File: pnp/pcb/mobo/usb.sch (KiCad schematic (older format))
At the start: 15 parts, among them J41 USB_B, J42 USB_A, J43 USB_A, J44 USB_A, U6 CH340G, U8 FE1.1S, Y2 12MHz, Y3 12MHz

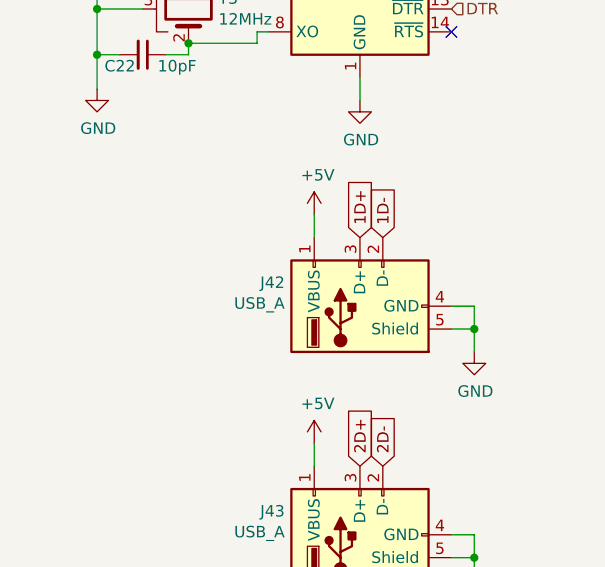
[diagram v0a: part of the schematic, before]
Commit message: Removing KiCad cache and bak files. Removing fabrication outputs. Updated Marlin to use the correct stepper driver for the Z and Y axis.
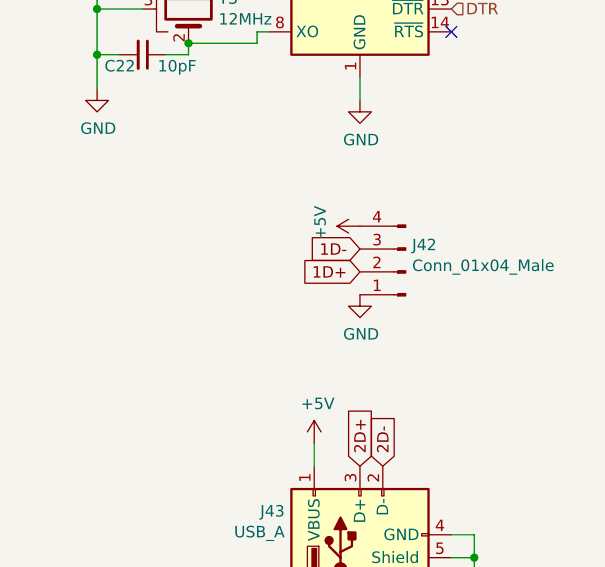
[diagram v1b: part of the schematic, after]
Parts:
- removed J42: USB_A, Connector_USB:USB_A_CNCTech_1001-011-01101_Horizontal, symbol Connector:USB_A
- added J42: Conn_01x04_Male, Connector_PinHeader_2.54mm:PinHeader_1x04_P2.54mm_Vertical, symbol Connector:Conn_01x04_Male
- J43, J44: footprint Connector_USB:USB_A_CNCTech_1001-011-01101_Horizontal -> Connector_USB:USB_A_Wuerth_61400826021_Horizontal_Stacked
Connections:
- net +5V: now also J42.4 (Pin_4)
- net 1D+: now also J42.2 (Pin_2)
- net 1D-: now also J42.3 (Pin_3)
- net GND: now also J42.1 (Pin_1)
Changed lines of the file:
@@
-$EndComp
-$Comp
-L Connector:USB_A J42
-U 1 1 5EB35624
-P 8650 3400
-F 0 "J42" V 8753 3729 50  0000 L CNN
-F 1 "USB_A" V 8662 3729 50  0000 L CNN
-F 2 "Connector_USB:USB_A_CNCTech_1001-011-01101_Horizontal" H 8800 3350 50  0001 C CNN
-F 3 " ~" H 8800 3350 50  0001 C CNN
-	1    8650 3400
-	0    -1   -1   0
 $EndComp
 $Comp
@@
 L power:GND #PWR0235
 U 1 1 5EB47F0D
-P 9150 3600
-F 0 "#PWR0235" H 9150 3350 50  0001 C CNN
-F 1 "GND" H 9155 3427 50  0000 C CNN
-F 2 "" H 9150 3600 50  0001 C CNN
-F 3 "" H 9150 3600 50  0001 C CNN
-	1    9150 3600
+P 8650 3350
+F 0 "#PWR0235" H 8650 3100 50  0001 C CNN
+F 1 "GND" H 8655 3177 50  0000 C CNN
+F 2 "" H 8650 3350 50  0001 C CNN
+F 3 "" H 8650 3350 50  0001 C CNN
+	1    8650 3350
 	1    0    0    -1
 $EndComp
@@
 	1    0    0    -1
 $EndComp
-Wire Wire Line
-	9150 3600 9150 3500
-Wire Wire Line
-	9150 3500 9050 3500
-Wire Wire Line
-	9150 3500 9150 3400
-Wire Wire Line
-	9150 3400 9050 3400
-Connection ~ 9150 3500
 $Comp
 L Connector:USB_A J43
@@
 F 0 "J43" V 8753 4729 50  0000 L CNN
 F 1 "USB_A" V 8662 4729 50  0000 L CNN
-F 2 "Connector_USB:USB_A_CNCTech_1001-011-01101_Horizontal" H 8800 4350 50  0001 C CNN
+F 2 "Connector_USB:USB_A_Wuerth_61400826021_Horizontal_Stacked" H 8800 4350 50  0001 C CNN
 F 3 " ~" H 8800 4350 50  0001 C CNN
 	1    8650 4400
@@
 F 0 "J44" V 8753 5879 50  0000 L CNN
 F 1 "USB_A" V 8662 5879 50  0000 L CNN
-F 2 "Connector_USB:USB_A_CNCTech_1001-011-01101_Horizontal" H 8800 5500 50  0001 C CNN
+F 2 "Connector_USB:USB_A_Wuerth_61400826021_Horizontal_Stacked" H 8800 5500 50  0001 C CNN
 F 3 " ~" H 8800 5500 50  0001 C CNN
 	1    8650 5550
@@
 L power:+5V #PWR0241
 U 1 1 5EB4E029
-P 8450 3000
-F 0 "#PWR0241" H 8450 2850 50  0001 C CNN
-F 1 "+5V" H 8465 3173 50  0000 C CNN
-F 2 "" H 8450 3000 50  0001 C CNN
-F 3 "" H 8450 3000 50  0001 C CNN
-	1    8450 3000
-	1    0    0    -1
+P 8650 3050
+F 0 "#PWR0241" H 8650 2900 50  0001 C CNN
+F 1 "+5V" H 8665 3223 50  0000 C CNN
+F 2 "" H 8650 3050 50  0001 C CNN
+F 3 "" H 8650 3050 50  0001 C CNN
+	1    8650 3050
+	0    -1   -1   0
 $EndComp
 $Comp
@@
 Wire Wire Line
 	8650 1200 8650 1100
-Wire Wire Line
-	8450 3100 8450 3000
 Wire Wire Line
 	8450 4100 8450 4000
@@
 Text GLabel 2100 3600 2    50   Input ~ 0
 MD+
-Text GLabel 8750 3100 1    50   Input ~ 0
+Text GLabel 8650 3150 0    50   Input ~ 0
 1D-
-Text GLabel 8650 3100 1    50   Input ~ 0
+Text GLabel 8650 3250 0    50   Input ~ 0
 1D+
 Text GLabel 8750 4100 1    50   Input ~ 0
@@
 	7500 2450 7500 2300
 Connection ~ 7500 2300
+$Comp
+L Connector:Conn_01x04_Male J42
+U 1 1 5EFACCD1
+P 8850 3250
+F 0 "J42" H 8822 3132 50  0000 R CNN
+F 1 "Conn_01x04_Male" H 8822 3223 50  0000 R CNN
+F 2 "Connector_PinHeader_2.54mm:PinHeader_1x04_P2.54mm_Vertical" H 8850 3250 50  0001 C CNN
+F 3 "~" H 8850 3250 50  0001 C CNN
+	1    8850 3250
+	-1   0    0    1
+$EndComp
 $EndSCHEMATC

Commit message: REV000 motherboard routing complete
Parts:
- removed J42: Conn_01x04_Male, Connector_PinHeader_2.54mm:PinHeader_1x04_P2.54mm_Vertical, symbol Connector:Conn_01x04_Male
- removed J43, J44: USB_A, Connector_USB:USB_A_Wuerth_61400826021_Horizontal_Stacked, symbol Connector:USB_A
- added J42: Conn_01x09_Male, Connector_USB:USB_A_Wuerth_61400826021_Horizontal_Stacked, symbol Connector:Conn_01x09_Male
- Y2, Y3: footprint (none) -> Crystal:Crystal_SMD_HC49-SD
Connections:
- net +5V: now also J42.1 (Pin_1), J42.5 (Pin_5)
- net 2D+: now also J42.3 (Pin_3)
- net 2D-: now also J42.2 (Pin_2)
- net 3D+: now also J42.7 (Pin_7)
- net 3D-: now also J42.6 (Pin_6)
- net GND: now also J42.4 (Pin_4), J42.8 (Pin_8), J42.9 (Pin_9)
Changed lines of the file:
@@
-$EndComp
-$Comp
-L power:GND #PWR0235
-U 1 1 5EB47F0D
-P 8650 3350
-F 0 "#PWR0235" H 8650 3100 50  0001 C CNN
-F 1 "GND" H 8655 3177 50  0000 C CNN
-F 2 "" H 8650 3350 50  0001 C CNN
-F 3 "" H 8650 3350 50  0001 C CNN
-	1    8650 3350
-	1    0    0    -1
 $EndComp
 $Comp
@@
 $EndComp
 $Comp
-L Connector:USB_A J43
-U 1 1 5EB49CAA
-P 8650 4400
-F 0 "J43" V 8753 4729 50  0000 L CNN
-F 1 "USB_A" V 8662 4729 50  0000 L CNN
-F 2 "Connector_USB:USB_A_Wuerth_61400826021_Horizontal_Stacked" H 8800 4350 50  0001 C CNN
-F 3 " ~" H 8800 4350 50  0001 C CNN
-	1    8650 4400
-	0    -1   -1   0
-$EndComp
-$Comp
 L power:GND #PWR0237
 U 1 1 5EB49CB4
-P 9150 4600
-F 0 "#PWR0237" H 9150 4350 50  0001 C CNN
-F 1 "GND" H 9155 4427 50  0000 C CNN
-F 2 "" H 9150 4600 50  0001 C CNN
-F 3 "" H 9150 4600 50  0001 C CNN
-	1    9150 4600
-	1    0    0    -1
-$EndComp
-Wire Wire Line
-	9150 4600 9150 4500
-Wire Wire Line
-	9150 4500 9050 4500
-Wire Wire Line
-	9150 4500 9150 4400
-Wire Wire Line
-	9150 4400 9050 4400
-Connection ~ 9150 4500
-$Comp
-L Connector:USB_A J44
-U 1 1 5EB4B7CF
-P 8650 5550
-F 0 "J44" V 8753 5879 50  0000 L CNN
-F 1 "USB_A" V 8662 5879 50  0000 L CNN
-F 2 "Connector_USB:USB_A_Wuerth_61400826021_Horizontal_Stacked" H 8800 5500 50  0001 C CNN
-F 3 " ~" H 8800 5500 50  0001 C CNN
-	1    8650 5550
-	0    -1   -1   0
+P 8250 3800
+F 0 "#PWR0237" H 8250 3550 50  0001 C CNN
+F 1 "GND" H 8300 3700 50  0000 C CNN
+F 2 "" H 8250 3800 50  0001 C CNN
+F 3 "" H 8250 3800 50  0001 C CNN
+	1    8250 3800
+	1    0    0    -1
 $EndComp
 $Comp
 L power:GND #PWR0238
 U 1 1 5EB4B7D9
-P 9150 5750
-F 0 "#PWR0238" H 9150 5500 50  0001 C CNN
-F 1 "GND" H 9155 5577 50  0000 C CNN
-F 2 "" H 9150 5750 50  0001 C CNN
-F 3 "" H 9150 5750 50  0001 C CNN
-	1    9150 5750
-	1    0    0    -1
-$EndComp
-Wire Wire Line
-	9150 5750 9150 5650
-Wire Wire Line
-	9150 5650 9050 5650
-Wire Wire Line
-	9150 5650 9150 5550
-Wire Wire Line
-	9150 5550 9050 5550
-Connection ~ 9150 5650
+P 8550 4350
+F 0 "#PWR0238" H 8550 4100 50  0001 C CNN
+F 1 "GND" H 8555 4177 50  0000 C CNN
+F 2 "" H 8550 4350 50  0001 C CNN
+F 3 "" H 8550 4350 50  0001 C CNN
+	1    8550 4350
+	1    0    0    -1
+$EndComp
 Wire Wire Line
 	8650 2500 8650 2400
@@
 $EndComp
 $Comp
-L power:+5V #PWR0241
-U 1 1 5EB4E029
-P 8650 3050
-F 0 "#PWR0241" H 8650 2900 50  0001 C CNN
-F 1 "+5V" H 8665 3223 50  0000 C CNN
-F 2 "" H 8650 3050 50  0001 C CNN
-F 3 "" H 8650 3050 50  0001 C CNN
-	1    8650 3050
-	0    -1   -1   0
-$EndComp
-$Comp
 L power:+5V #PWR0242
 U 1 1 5EB4E617
-P 8450 4000
-F 0 "#PWR0242" H 8450 3850 50  0001 C CNN
-F 1 "+5V" H 8465 4173 50  0000 C CNN
-F 2 "" H 8450 4000 50  0001 C CNN
-F 3 "" H 8450 4000 50  0001 C CNN
-	1    8450 4000
+P 8050 3950
+F 0 "#PWR0242" H 8050 3800 50  0001 C CNN
+F 1 "+5V" H 8065 4123 50  0000 C CNN
+F 2 "" H 8050 3950 50  0001 C CNN
+F 3 "" H 8050 3950 50  0001 C CNN
+	1    8050 3950
 	1    0    0    -1
 $EndComp
@@
 L power:+5V #PWR0243
 U 1 1 5EB4E911
-P 8450 5150
-F 0 "#PWR0243" H 8450 5000 50  0001 C CNN
-F 1 "+5V" H 8465 5323 50  0000 C CNN
-F 2 "" H 8450 5150 50  0001 C CNN
-F 3 "" H 8450 5150 50  0001 C CNN
-	1    8450 5150
+P 8550 3550
+F 0 "#PWR0243" H 8550 3400 50  0001 C CNN
+F 1 "+5V" H 8565 3723 50  0000 C CNN
+F 2 "" H 8550 3550 50  0001 C CNN
+F 3 "" H 8550 3550 50  0001 C CNN
+	1    8550 3550
 	1    0    0    -1
 $EndComp
 Wire Wire Line
 	8650 1200 8650 1100
-Wire Wire Line
-	8450 4100 8450 4000
-Wire Wire Line
-	8450 5250 8450 5150
 Wire Wire Line
 	2100 3400 2200 3400
@@
 	1    0    0    -1
 $EndComp
-Text HLabel 2050 1300 0    50   Input ~ 0
-5v
-Text HLabel 2300 1300 2    50   Input ~ 0
-12v
-Text HLabel 1700 1300 0    50   Input ~ 0
-GND
 $Comp
 L power:GND #PWR0246
@@
 F 0 "Y2" V 3304 2681 50  0000 L CNN
 F 1 "12MHz" V 3395 2681 50  0000 L CNN
-F 2 "" H 3350 2550 50  0001 C CNN
+F 2 "Crystal:Crystal_SMD_HC49-SD" H 3350 2550 50  0001 C CNN
 F 3 "~" H 3350 2550 50  0001 C CNN
 	1    3350 2550
@@
 Text GLabel 2100 3600 2    50   Input ~ 0
 MD+
-Text GLabel 8650 3150 0    50   Input ~ 0
-1D-
-Text GLabel 8650 3250 0    50   Input ~ 0
-1D+
-Text GLabel 8750 4100 1    50   Input ~ 0
+Text GLabel 8550 3650 0    50   Input ~ 0
 2D-
-Text GLabel 8650 4100 1    50   Input ~ 0
+Text GLabel 8550 3750 0    50   Input ~ 0
 2D+
-Text GLabel 8750 5250 1    50   Input ~ 0
+Text GLabel 8550 4050 0    50   Input ~ 0
 3D-
-Text GLabel 8650 5250 1    50   Input ~ 0
+Text GLabel 8550 4150 0    50   Input ~ 0
 3D+
 Text GLabel 8250 1800 0    50   Input ~ 0
@@
 Text GLabel 8250 1700 0    50   Input ~ 0
 4D+
-Text HLabel 9050 1400 2    50   Input ~ 0
-TX
-Text HLabel 9050 1500 2    50   Input ~ 0
-RX
 NoConn ~ 8250 1500
 NoConn ~ 9050 2200
@@
 NoConn ~ 9050 1800
 NoConn ~ 9050 1900
-Text HLabel 9050 1700 2    50   Input ~ 0
-CTS
-Text HLabel 9050 2100 2    50   Input ~ 0
-DTR
 $Comp
 L Device:C_Small C23
@@
 F 0 "Y3" V 7854 2231 50  0000 L CNN
 F 1 "12MHz" V 7945 2231 50  0000 L CNN
-F 2 "" H 7900 2100 50  0001 C CNN
+F 2 "Crystal:Crystal_SMD_HC49-SD" H 7900 2100 50  0001 C CNN
 F 3 "~" H 7900 2100 50  0001 C CNN
 	1    7900 2100
@@
 	7500 2450 7500 2300
 Connection ~ 7500 2300
-$Comp
-L Connector:Conn_01x04_Male J42
-U 1 1 5EFACCD1
-P 8850 3250
-F 0 "J42" H 8822 3132 50  0000 R CNN
-F 1 "Conn_01x04_Male" H 8822 3223 50  0000 R CNN
-F 2 "Connector_PinHeader_2.54mm:PinHeader_1x04_P2.54mm_Vertical" H 8850 3250 50  0001 C CNN
-F 3 "~" H 8850 3250 50  0001 C CNN
-	1    8850 3250
-	-1   0    0    1
-$EndComp
+Text GLabel 1700 1300 0    50   Input ~ 0
+GND
+Text GLabel 2050 1300 0    50   Input ~ 0
+5v
+Text GLabel 2300 1300 2    50   Input ~ 0
+12v
+Text GLabel 9050 2100 2    50   Input ~ 0
+DTR
+Text GLabel 9050 1700 2    50   Input ~ 0
+CTS
+Text GLabel 9050 1500 2    50   Input ~ 0
+RX
+Text GLabel 9050 1400 2    50   Input ~ 0
+TX
+$Comp
+L Connector:Conn_01x09_Male J42
+U 1 1 5ED3225B
+P 8750 3950
+F 0 "J42" H 8722 3974 50  0000 R CNN
+F 1 "Conn_01x09_Male" H 8722 3883 50  0000 R CNN
+F 2 "Connector_USB:USB_A_Wuerth_61400826021_Horizontal_Stacked" H 8750 3950 50  0001 C CNN
+F 3 "~" H 8750 3950 50  0001 C CNN
+	1    8750 3950
+	-1   0    0    -1
+$EndComp
+Wire Wire Line
+	8050 3950 8550 3950
+Wire Wire Line
+	8250 3800 8400 3800
+Wire Wire Line
+	8400 3800 8400 3850
+Wire Wire Line
+	8400 3850 8550 3850
+Wire Wire Line
+	8550 4250 8550 4350
+Connection ~ 8550 4350
 $EndSCHEMATC

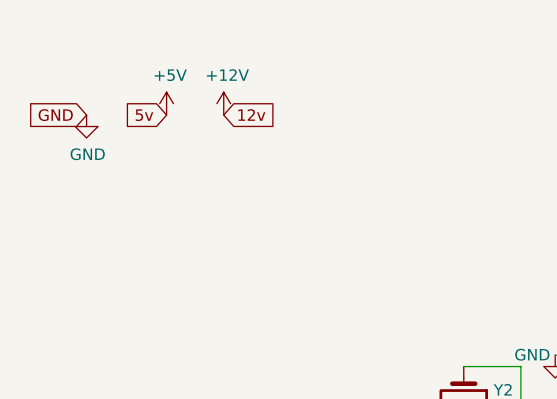
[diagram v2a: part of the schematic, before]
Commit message: Clean up Main PCB symbology
there is still an issue with the USB hub chip not working correctly, as it is reliant on a library outside the working folder structure
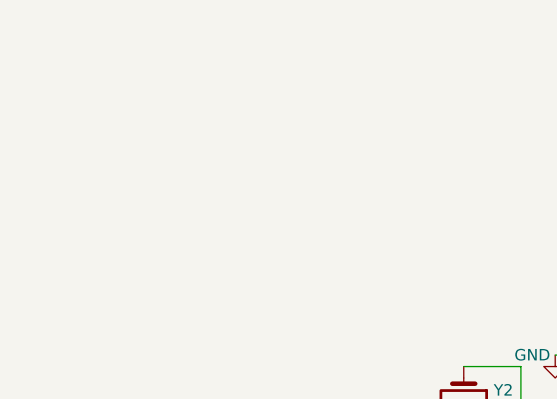
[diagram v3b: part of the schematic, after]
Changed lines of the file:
@@
 EESchema Schematic File Version 4
+LIBS:mobo-cache
 EELAYER 30 0
 EELAYER END
@@
 Wire Wire Line
 	1700 4100 1700 4000
-$Comp
-L power:+5V #PWR0244
-U 1 1 5EB51396
-P 2050 1300
-F 0 "#PWR0244" H 2050 1150 50  0001 C CNN
-F 1 "+5V" H 2065 1473 50  0000 C CNN
-F 2 "" H 2050 1300 50  0001 C CNN
-F 3 "" H 2050 1300 50  0001 C CNN
-	1    2050 1300
-	1    0    0    -1
-$EndComp
-$Comp
-L power:+12V #PWR0245
-U 1 1 5EB5139C
-P 2300 1300
-F 0 "#PWR0245" H 2300 1150 50  0001 C CNN
-F 1 "+12V" H 2315 1473 50  0000 C CNN
-F 2 "" H 2300 1300 50  0001 C CNN
-F 3 "" H 2300 1300 50  0001 C CNN
-	1    2300 1300
-	1    0    0    -1
-$EndComp
-$Comp
-L power:GND #PWR0246
-U 1 1 5EB513A5
-P 1700 1300
-F 0 "#PWR0246" H 1700 1050 50  0001 C CNN
-F 1 "GND" H 1705 1127 50  0000 C CNN
-F 2 "" H 1700 1300 50  0001 C CNN
-F 3 "" H 1700 1300 50  0001 C CNN
-	1    1700 1300
-	1    0    0    -1
-$EndComp
 $Comp
 L index:FE1.1S U8
@@
 	7500 2450 7500 2300
 Connection ~ 7500 2300
-Text GLabel 1700 1300 0    50   Input ~ 0
-GND
-Text GLabel 2050 1300 0    50   Input ~ 0
-5v
-Text GLabel 2300 1300 2    50   Input ~ 0
-12v
 Text GLabel 9050 2100 2    50   Input ~ 0
 DTR
